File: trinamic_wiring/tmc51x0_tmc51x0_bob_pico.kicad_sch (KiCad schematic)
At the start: 3 parts, among them M1 Stepper_Motor

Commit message: Add pico
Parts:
- removed A1: TEENSY_4.0_HEADERS, Janelia:TEENSY_4.0_HEADERS, symbol Janelia:TEENSY_4.0_HEADERS
- added A3: PICO_HEADERS, Janelia:PICO_HEADERS, symbol Janelia:PICO_HEADERS
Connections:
- net CS: now also A3.14 (I2C1-SDA/SPI1-SCK/GP10)
- net GND: now also A3.23 (GND)
- net MISO: now also A3.26 (I2C0-SDA/GP20)
- net MOSI: now also A3.25 (I2C1-SCL/SPI0-TX/GP19)
- net SCK: now also A3.24 (I2C1-SDA/SPI0-SCK/GP18)
- net VIO: now also A3.36 (3V3(OUT))
- net ~{HARDWARE_ENABLE}: now also A3.6 (UART1-TX/I2C0-SDA/SPI0-RX/GP4)
- no-connect marks 29 -> 41

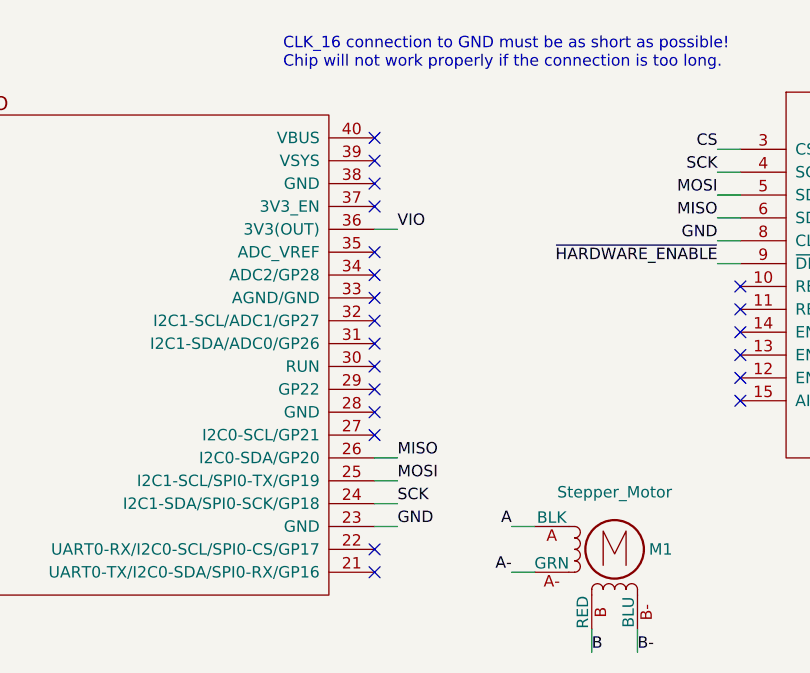
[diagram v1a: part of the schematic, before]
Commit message: Move ground pin
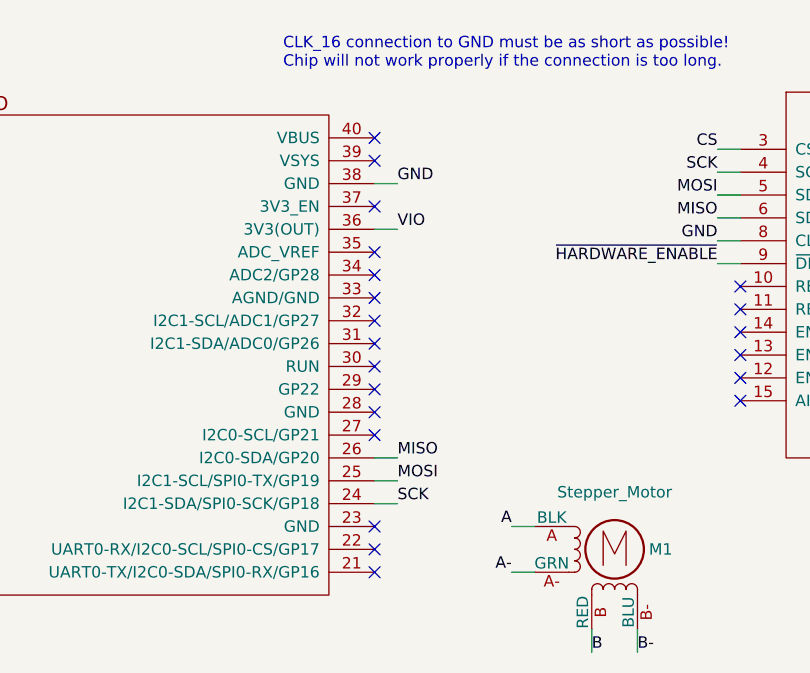
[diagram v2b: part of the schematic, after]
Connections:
- net GND: now also A3.38 (GND); no longer A3.23 (GND)
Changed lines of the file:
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@@
   (no_connect (at 163.83 114.3))
   (no_connect (at 123.19 87.63))
+  (no_connect (at 123.19 130.81))
   (no_connect (at 36.83 115.57))
   (no_connect (at 36.83 125.73))
   (no_connect (at 163.83 104.14))
   (no_connect (at 163.83 109.22))
-  (no_connect (at 123.19 92.71))
   (no_connect (at 163.83 106.68))
   (no_connect (at 36.83 128.27))
@@
     (stroke (width 0) (type default))
   )
-  (wire (pts (xy 125.73 130.81) (xy 123.19 130.81))
+  (wire (pts (xy 125.73 92.71) (xy 123.19 92.71))
     (stroke (width 0) (type default))
   )
@@
     (effects (font (size 1.27 1.27)) (justify left bottom))
   )
-  (label "GND" (at 125.73 130.81 0) (fields_autoplaced)
+  (label "GND" (at 125.73 92.71 0) (fields_autoplaced)
     (effects (font (size 1.27 1.27)) (justify left bottom))
   )
@@
     (instances
       (project "trinamic_wiring"
-        (path "/e4144788-6304-493f-818e-5d881d3b7418/a161638e-a96f-4455-865a-1d7502675f43/176cb0b5-cab1-47ac-9998-e59b71e39393/106cbaaa-dd32-4d4d-a442-e3c42a8253b0"
-          (reference "BOB1") (unit 1)
-        )
         (path "/e4144788-6304-493f-818e-5d881d3b7418/a161638e-a96f-4455-865a-1d7502675f43/176cb0b5-cab1-47ac-9998-e59b71e39393/dab15df5-b51f-4c1f-8fc9-49b45f8778bf"
           (reference "BOB1") (unit 1)
@@
     (instances
       (project "trinamic_wiring"
-        (path "/e4144788-6304-493f-818e-5d881d3b7418/a161638e-a96f-4455-865a-1d7502675f43/176cb0b5-cab1-47ac-9998-e59b71e39393/106cbaaa-dd32-4d4d-a442-e3c42a8253b0"
-          (reference "M1") (unit 1)
-        )
         (path "/e4144788-6304-493f-818e-5d881d3b7418/a161638e-a96f-4455-865a-1d7502675f43/176cb0b5-cab1-47ac-9998-e59b71e39393/dab15df5-b51f-4c1f-8fc9-49b45f8778bf"
           (reference "M1") (unit 1)
